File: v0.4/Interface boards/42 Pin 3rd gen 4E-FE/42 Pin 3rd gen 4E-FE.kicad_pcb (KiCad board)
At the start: 2 copper layers, 50.7 x 79.4 mm, 7 parts, among them J1 4E-FE OEM, J2 KNOCK, J3 Speeduino, J5 Conn_01x02, J6 STARTER

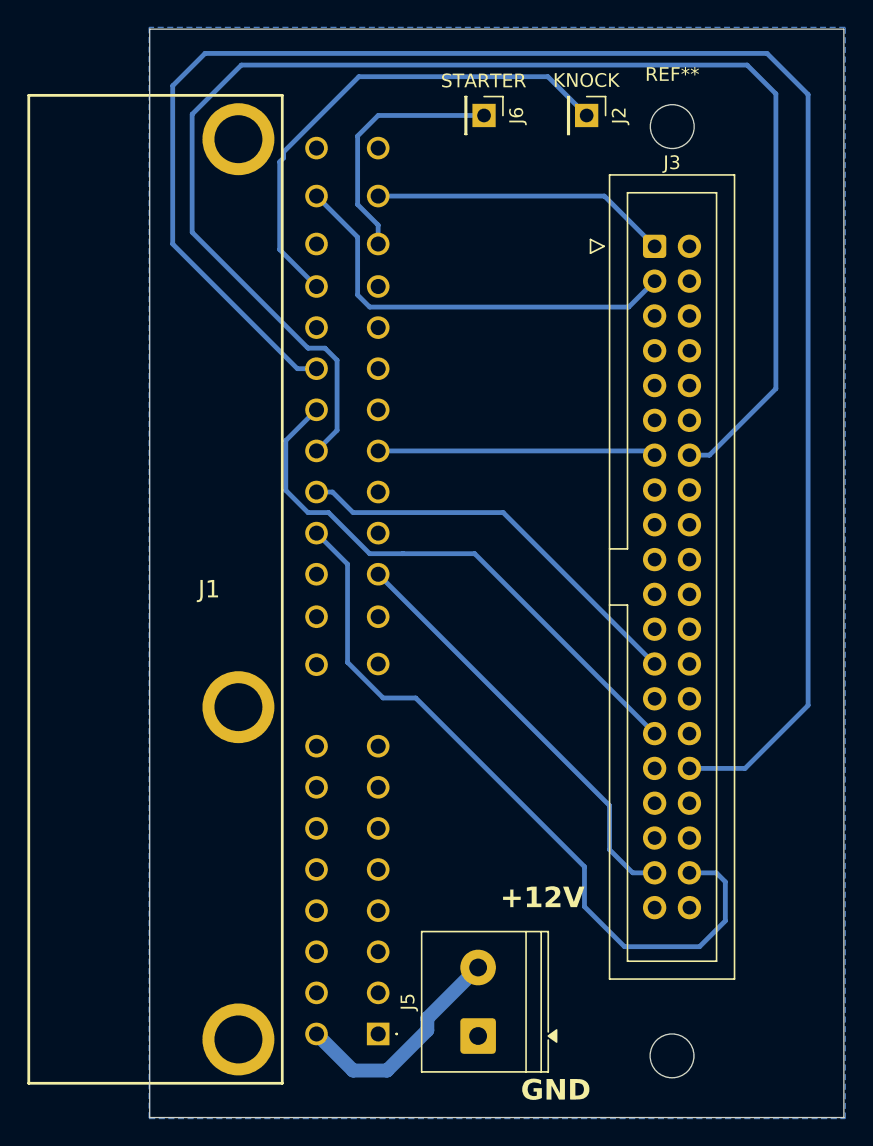
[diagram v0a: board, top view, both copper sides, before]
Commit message: Updated Interface board to include VR pickup negative side. Added ground plane to top side.
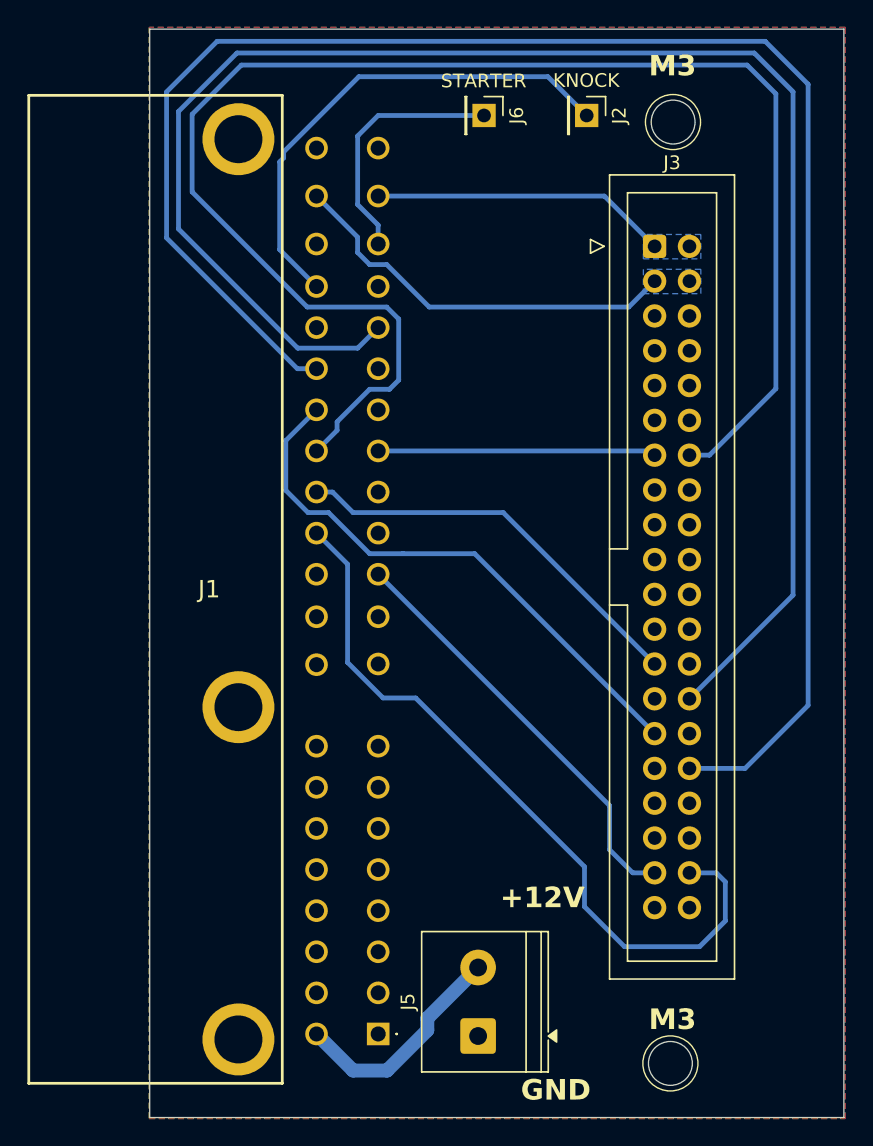
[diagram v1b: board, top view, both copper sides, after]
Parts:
- removed the REF** at (132.5, 70.2)
- added REF**: MountingHole_3.2mm_M3_DIN965, MountingHole:MountingHole_3.2mm_M3_DIN965, F.Cu at (132.4, 138.6)
- moved ? 68.1 mm to (132.6, 69.9)
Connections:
- J3 pad 2: unconnected-(J3-Pin_2-Pad2) -> #10
- J3 pad 28: unconnected-(J3-Pin_28-Pad28) -> NE-
- J3 pad 4: unconnected-(J3-Pin_4-Pad4) -> #20
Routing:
- net NE-: track 0.00 -> 122.6 mm
- net IGT2: track 105.1 -> 112.3 mm
- net #20: track 31.3 -> 29.5 mm
- net NE: track 129.5 -> 131.1 mm
- added copper zone on B.Cu, net #10
- added copper zone on B.Cu, net #20
- added copper zone on F.Cu, net E1
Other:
- board text added: "M3"
